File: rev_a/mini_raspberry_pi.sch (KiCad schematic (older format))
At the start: 4 parts

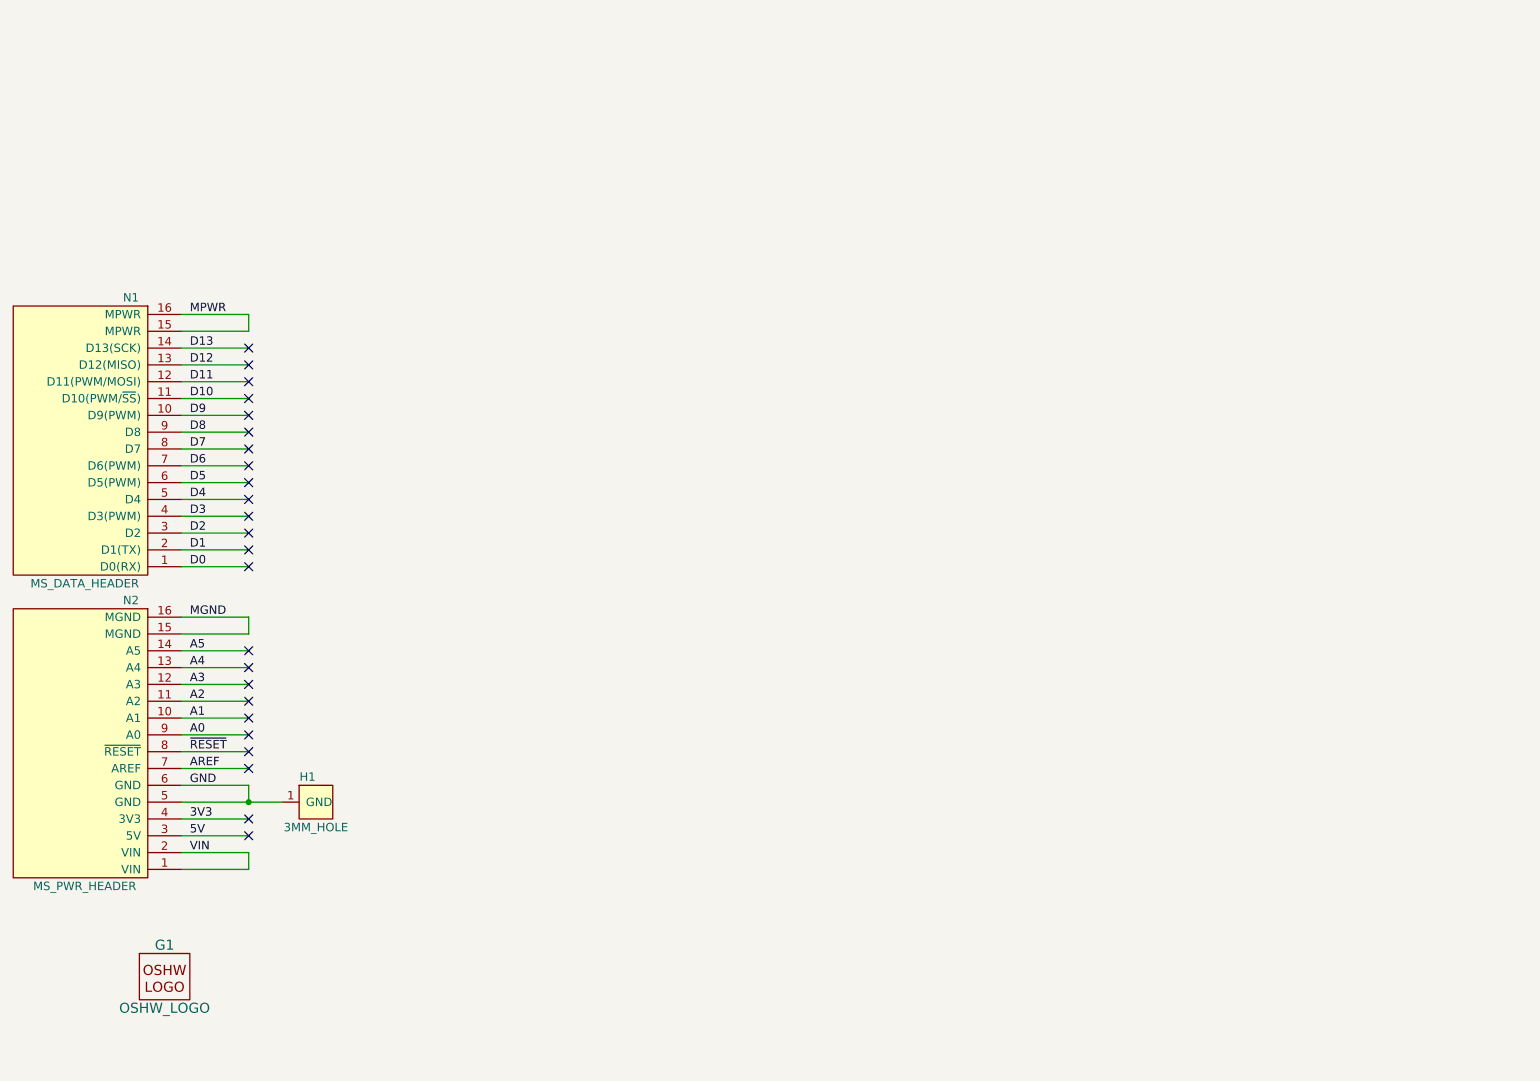
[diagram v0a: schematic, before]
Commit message: Layed out PCB for Raspberry Pi Mini-Shield
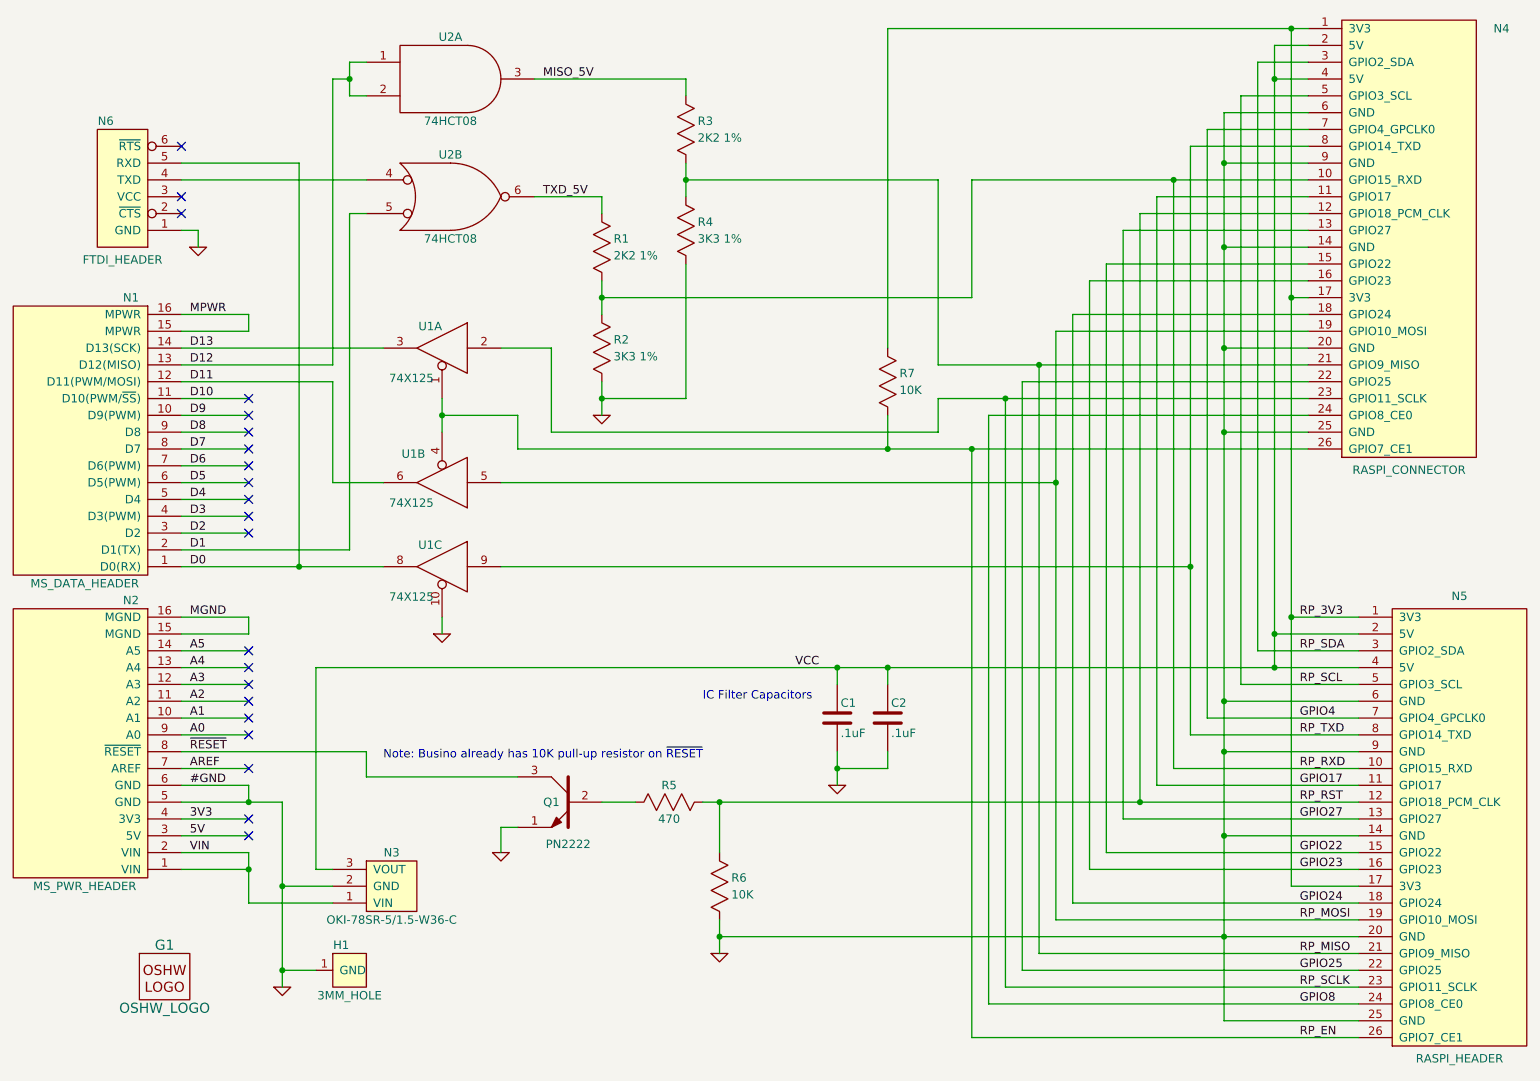
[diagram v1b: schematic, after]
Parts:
- added C1, C2: .1uF, symbol C_VERT
- added N3: OKI-78SR-5/1.5-W36-C, symbol REGULATOR_CONNECTOR
- added N4: RASPI_CONNECTOR, symbol RASPI_CONNECTOR
- added N5: RASPI_HEADER, symbol RASPI_HEADER
- added N6: FTDI_HEADER, symbol FTDI_HEADER
- added Q1: PN2222, symbol NPN
- added R1, R3: 2K2 1%, symbol R_VERT
- added R2, R4: 3K3 1%, symbol R_VERT
- added R5: 470, symbol R_HORIZ
- added R6, R7: 10K, symbol R_VERT
- added U1: 74X125, symbol 74X125
- added U2: 74HCT08, symbol 74X08
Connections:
- net D0: now also N6.5 (RXD), U1.8
- net D1: now also U2.5
- net D11: now also U1.6
- net D12: now also U2.1, U2.2
- net D13: now also U1.3
- net GND: now also C1.2, C2.2, N3.2 (GND), N4.14 (GND), N4.20 (GND), N4.25 (GND), N4.6 (GND), N4.9 (GND), N5.14 (GND), N5.20 (GND), N5.25 (GND), N5.6 (GND), N5.9 (GND), N6.1 (GND), Q1.1, R2.1, R4.1, R6.1, U1.10, U1.7 (GND), U1.7 (GND), U1.7 (GND), U2.7 (GND), U2.7 (GND)
- net VIN: now also N3.1 (VIN)
- net ~RESET: now also Q1.3
- new net: Q1.2, R5.1
- new net: N6.4 (TXD), U2.4
- new net GPIO17: N4.11 (GPIO17), N5.11 (GPIO17)
- new net GPIO22: N4.15 (GPIO22), N5.15 (GPIO22)
- new net GPIO23: N4.16 (GPIO23), N5.16 (GPIO23)
- new net GPIO24: N4.18 (GPIO24), N5.18 (GPIO24)
- new net GPIO25: N4.22 (GPIO25), N5.22 (GPIO25)
- new net GPIO27: N4.13 (GPIO27), N5.13 (GPIO27)
- new net GPIO4: N4.7 (GPIO4_GPCLK0), N5.7 (GPIO4_GPCLK0)
- new net GPIO8: N4.24 (GPIO8_CE0), N5.24 (GPIO8_CE0)
- new net MISO_5V: R3.2, U2.3
- new net RP_3V3: N4.1 (3V3), N4.17 (3V3), N5.1 (3V3), N5.17 (3V3), R7.2
- new net RP_EN: N4.26 (GPIO7_CE1), N5.26 (GPIO7_CE1), R7.1, U1.1, U1.4
- new net RP_MISO: N4.21 (GPIO9_MISO), N5.21 (GPIO9_MISO), R3.1, R4.2
- new net RP_MOSI: N4.19 (GPIO10_MOSI), N5.19 (GPIO10_MOSI), U1.5
- new net RP_RST: N4.12 (GPIO18_PCM_CLK), N5.12 (GPIO18_PCM_CLK), R5.2, R6.2
- new net RP_RXD: N4.10 (GPIO15_RXD), N5.10 (GPIO15_RXD), R1.1, R2.2
- new net RP_SCL: N4.5 (GPIO3_SCL), N5.5 (GPIO3_SCL)
- new net RP_SCLK: N4.23 (GPIO11_SCLK), N5.23 (GPIO11_SCLK), U1.2
- new net RP_SDA: N4.3 (GPIO2_SDA), N5.3 (GPIO2_SDA)
- new net RP_TXD: N4.8 (GPIO14_TXD), N5.8 (GPIO14_TXD), U1.9
- new net TXD_5V: R1.2, U2.6
- new net VCC: C1.1, C2.1, N3.3 (VOUT), N4.2 (5V), N4.4 (5V), N5.2 (5V), N5.4 (5V), U1.14 (VCC), U1.14 (VCC), U1.14 (VCC), U2.14 (VCC), U2.14 (VCC)
- no-connect marks 24 -> 21
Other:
- note added: "IC Filter Capacitors"
- note added: "Note: Busino already has 10K pull-up resistor on ~RESET"
- moved on the sheet: H1
